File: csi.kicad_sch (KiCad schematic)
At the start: 61 parts, among them J7 WE_68715014522_ONE-SIDE, J8 WE_68715014522_ONE-SIDE, U24 AP22653FDZ-7, U25 AP22653FDZ-7, U26 PCA9547BS, U27 AP22653FDZ-7, U28 AP22653FDZ-7, U31 NTS0102GT, U32 NTS0102GT

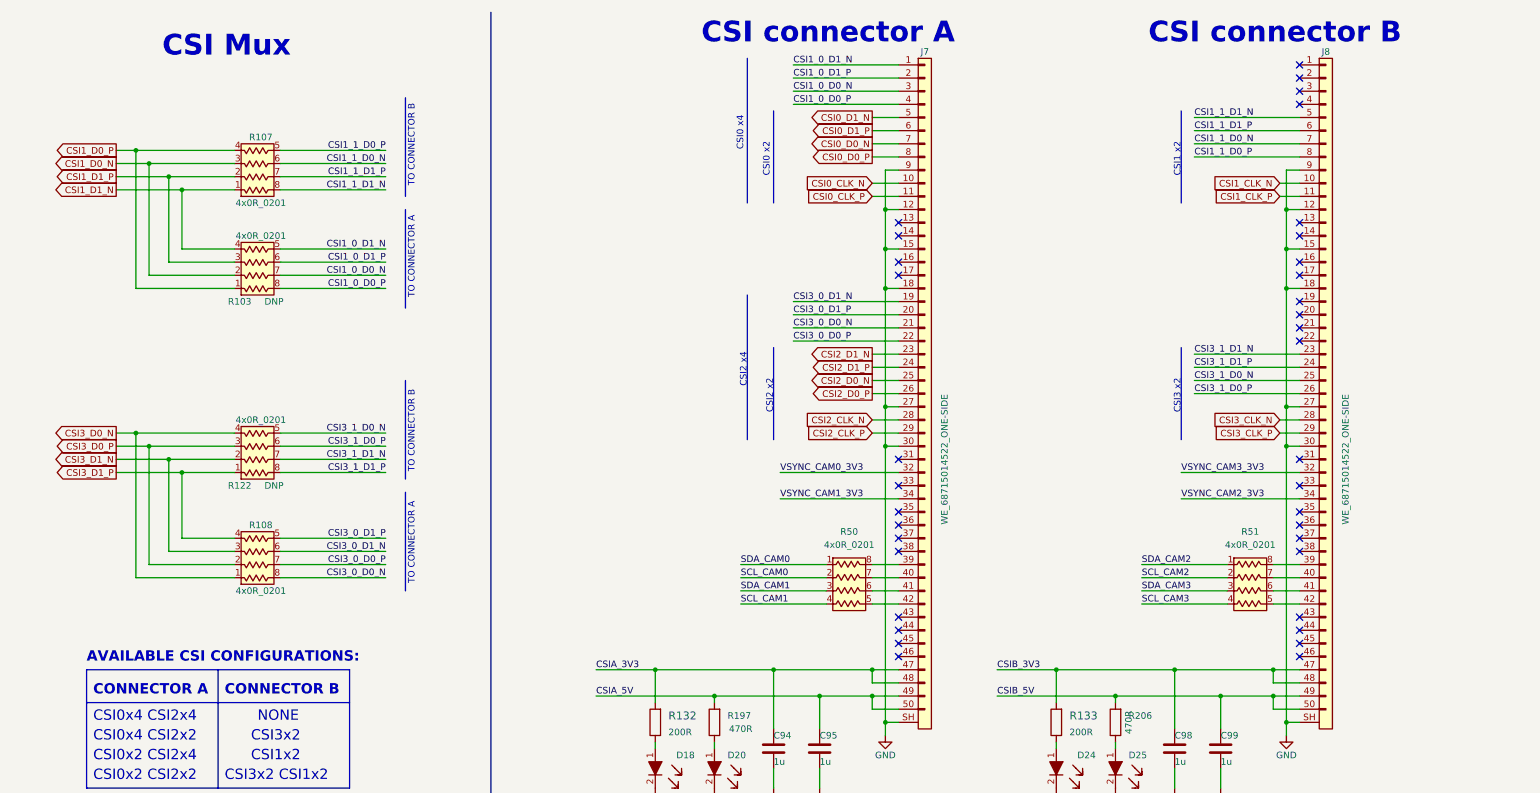
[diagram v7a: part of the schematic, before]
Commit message: Update CSI connector naming
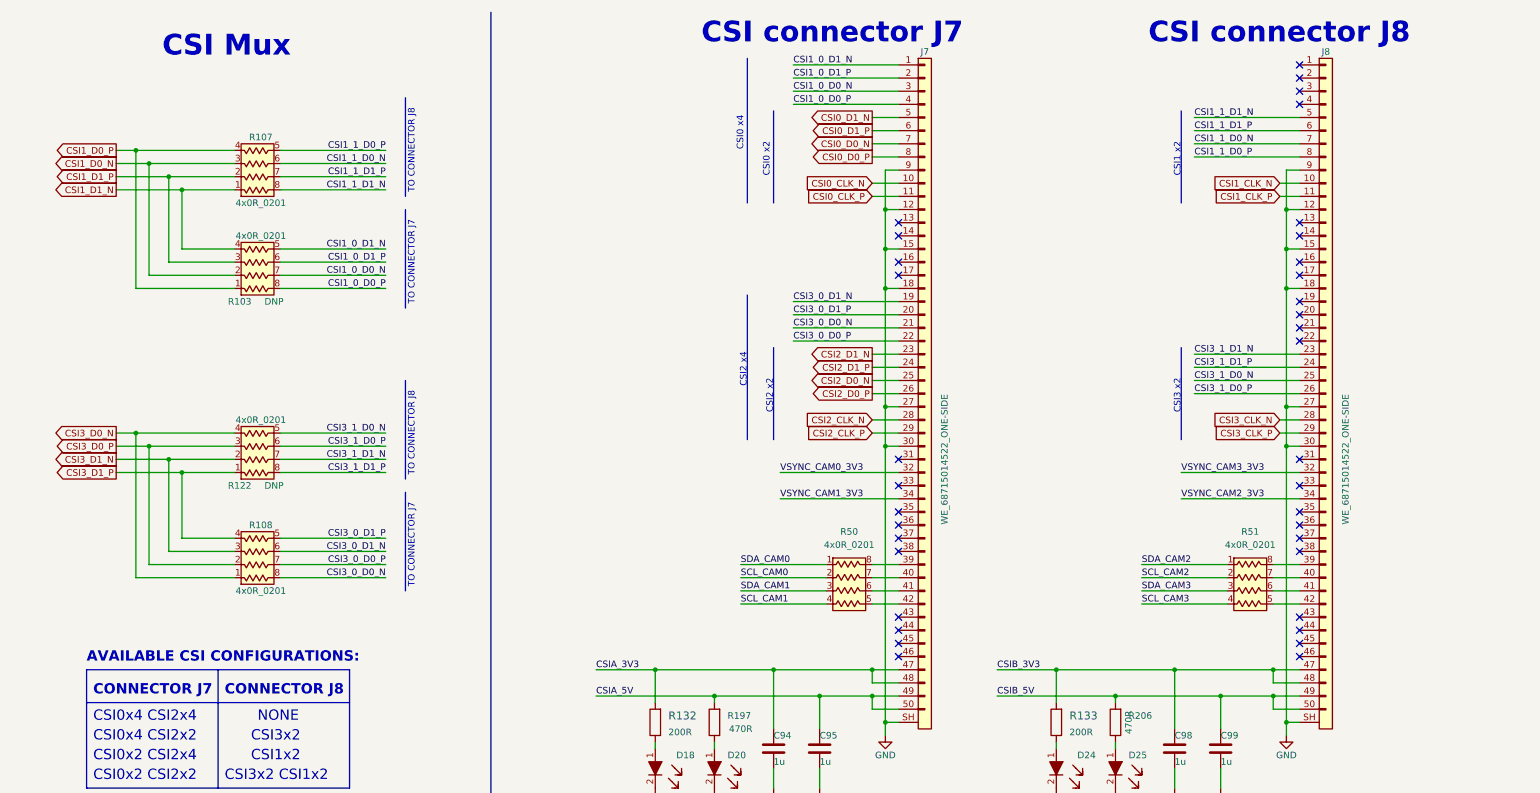
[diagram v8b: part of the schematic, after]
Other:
- note added: "CONNECTOR J7"
- note added: "CONNECTOR J8"
- note added: "CSI connector J7"
- note added: "CSI connector J8"
- note added: "TO CONNECTOR J7"
- note added: "TO CONNECTOR J8"
- note removed: "CONNECTOR A"
- note removed: "CONNECTOR B"
- note removed: "CSI connector A"
- note removed: "CSI connector B"
- note removed: "TO CONNECTOR A"
- note removed: "TO CONNECTOR B"
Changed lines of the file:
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@@
     )
   )
-  (text "CONNECTOR B\n" (at 155.575 144.78 0)
+  (text "CONNECTOR J8\n" (at 155.575 144.78 0)
     (effects (font (size 2 2) (thickness 0.4) bold) (justify left bottom))
   )
@@
     (effects (font (size 2 2)) (justify left bottom))
   )
-  (text "CONNECTOR A" (at 130.175 144.78 0)
+  (text "CONNECTOR J7" (at 130.175 144.78 0)
     (effects (font (size 2 2) (thickness 0.4) bold) (justify left bottom))
   )
@@
     (effects (font (size 2 2)) (justify left bottom))
   )
-  (text "TO CONNECTOR A" (at 192.405 67.945 90)
+  (text "TO CONNECTOR J7" (at 192.405 69.215 90)
     (effects (font (size 1.27 1.27)) (justify left bottom))
   )
@@
     (effects (font (size 1.27 1.27)) (justify left bottom))
   )
-  (text "TO CONNECTOR B\n" (at 192.405 46.355 90)
+  (text "TO CONNECTOR J8\n" (at 192.405 47.625 90)
     (effects (font (size 1.27 1.27)) (justify left bottom))
   )
@@
     (effects (font (size 4 4) (thickness 0.8) bold) (justify left bottom))
   )
-  (text "CSI connector A" (at 247.65 19.05 0)
+  (text "CSI connector J7" (at 247.65 19.05 0)
     (effects (font (size 4 4) (thickness 0.8) bold) (justify left bottom))
   )
@@
     (effects (font (size 2 2)) (justify left bottom))
   )
-  (text "TO CONNECTOR B\n" (at 192.405 101.6 90)
+  (text "TO CONNECTOR J8\n" (at 192.405 102.235 90)
     (effects (font (size 1.27 1.27)) (justify left bottom))
   )
-  (text "TO CONNECTOR A" (at 192.405 123.19 90)
+  (text "TO CONNECTOR J7" (at 192.405 123.825 90)
     (effects (font (size 1.27 1.27)) (justify left bottom))
   )
@@
     (effects (font (size 4 4) (thickness 0.8) bold) (justify left bottom))
   )
-  (text "CSI connector B" (at 334.01 19.05 0)
+  (text "CSI connector J8" (at 334.01 19.05 0)
     (effects (font (size 4 4) (thickness 0.8) bold) (justify left bottom))
   )
